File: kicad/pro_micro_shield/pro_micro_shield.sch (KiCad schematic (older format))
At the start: 14 parts, among them U0 ProMicro

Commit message: cleanup shield kicad project and readme
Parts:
- added H0, H1: MountingHole, MountingHole:MountingHole_2.2mm_M2, symbol Mechanical:MountingHole
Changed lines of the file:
@@
+	1    0    0    -1
+$EndComp
+$Comp
+L Mechanical:MountingHole H0
+U 1 1 5E6408C2
+P 7350 4550
+F 0 "H0" H 7450 4596 50  0000 L CNN
+F 1 "MountingHole" H 7450 4505 50  0000 L CNN
+F 2 "MountingHole:MountingHole_2.2mm_M2" H 7350 4550 50  0001 C CNN
+F 3 "~" H 7350 4550 50  0001 C CNN
+	1    7350 4550
+	1    0    0    -1
+$EndComp
+$Comp
+L Mechanical:MountingHole H1
+U 1 1 5E640F0D
+P 7350 4800
+F 0 "H1" H 7450 4846 50  0000 L CNN
+F 1 "MountingHole" H 7450 4755 50  0000 L CNN
+F 2 "MountingHole:MountingHole_2.2mm_M2" H 7350 4800 50  0001 C CNN
+F 3 "~" H 7350 4800 50  0001 C CNN
+	1    7350 4800
 	1    0    0    -1
 $EndComp

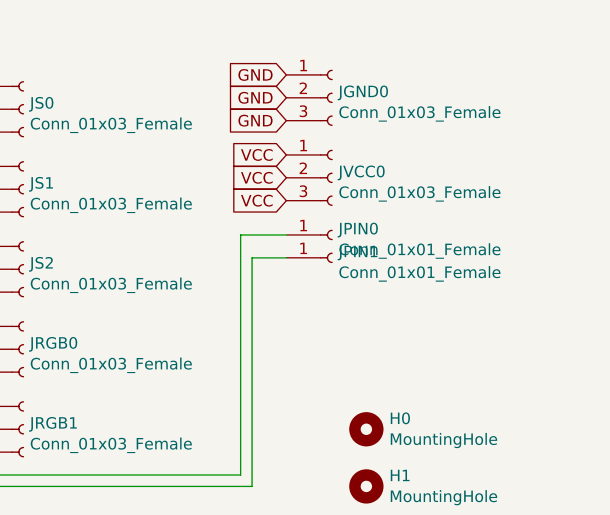
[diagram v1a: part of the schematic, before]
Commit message: cleanup shield kicad project and readme
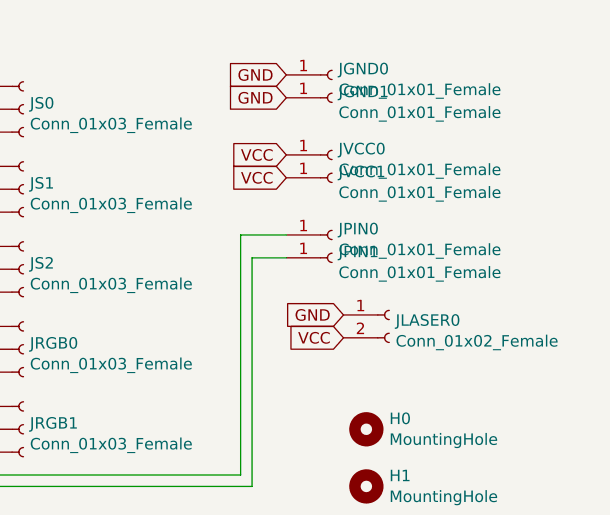
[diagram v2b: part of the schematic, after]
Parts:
- removed JGND0, JVCC0: Conn_01x03_Female, Connector_Wire:SolderWirePad_1x03_P3.175mm_Drill1mm, symbol Connector:Conn_01x03_Female
- added JGND0, JGND1, JVCC0, JVCC1: Conn_01x01_Female, Connector_Wire:SolderWirePad_1x01_Drill1mm, symbol Connector:Conn_01x01_Female
- added JLASER0: Conn_01x02_Female, Connector_Wire:SolderWirePad_1x02_P3.81mm_Drill1mm, symbol Connector:Conn_01x02_Female
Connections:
- net GND: now also JGND0.1 (Pin_1), JGND1.1 (Pin_1), JLASER0.1 (Pin_1)
- net VCC: now also JLASER0.2 (Pin_2), JVCC0.1 (Pin_1), JVCC1.1 (Pin_1)
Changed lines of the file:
@@
 Wire Wire Line
 	5200 5200 3150 5200
-$Comp
-L Connector:Conn_01x03_Female JGND0
-U 1 1 5E645A68
-P 7200 3100
-F 0 "JGND0" H 7228 3126 50  0000 L CNN
-F 1 "Conn_01x03_Female" H 7228 3035 50  0000 L CNN
-F 2 "Connector_Wire:SolderWirePad_1x03_P3.175mm_Drill1mm" H 7200 3100 50  0001 C CNN
-F 3 "~" H 7200 3100 50  0001 C CNN
-	1    7200 3100
-	1    0    0    -1
-$EndComp
-$Comp
-L Connector:Conn_01x03_Female JVCC0
-U 1 1 5E6468D3
-P 7200 3450
-F 0 "JVCC0" H 7228 3476 50  0000 L CNN
-F 1 "Conn_01x03_Female" H 7228 3385 50  0000 L CNN
-F 2 "Connector_Wire:SolderWirePad_1x03_P3.175mm_Drill1mm" H 7200 3450 50  0001 C CNN
-F 3 "~" H 7200 3450 50  0001 C CNN
-	1    7200 3450
-	1    0    0    -1
-$EndComp
 Text GLabel 7000 3000 0    50   Input ~ 0
 GND
 Text GLabel 7000 3100 0    50   Input ~ 0
 GND
-Text GLabel 7000 3200 0    50   Input ~ 0
-GND
 Text GLabel 7000 3350 0    50   Input ~ 0
 VCC
 Text GLabel 7000 3450 0    50   Input ~ 0
-VCC
-Text GLabel 7000 3550 0    50   Input ~ 0
 VCC
 Wire Wire Line
@@
 	1    0    0    -1
 $EndComp
+$Comp
+L Connector:Conn_01x02_Female JLASER0
+U 1 1 5E661891
+P 7450 4050
+F 0 "JLASER0" H 7478 4026 50  0000 L CNN
+F 1 "Conn_01x02_Female" H 7478 3935 50  0000 L CNN
+F 2 "Connector_Wire:SolderWirePad_1x02_P3.81mm_Drill1mm" H 7450 4050 50  0001 C CNN
+F 3 "~" H 7450 4050 50  0001 C CNN
+	1    7450 4050
+	1    0    0    -1
+$EndComp
+Text GLabel 7250 4150 0    50   Input ~ 0
+VCC
+Text GLabel 7250 4050 0    50   Input ~ 0
+GND
+$Comp
+L Connector:Conn_01x01_Female JGND0
+U 1 1 5E666EF2
+P 7200 3000
+F 0 "JGND0" H 7228 3026 50  0000 L CNN
+F 1 "Conn_01x01_Female" H 7228 2935 50  0000 L CNN
+F 2 "Connector_Wire:SolderWirePad_1x01_Drill1mm" H 7200 3000 50  0001 C CNN
+F 3 "~" H 7200 3000 50  0001 C CNN
+	1    7200 3000
+	1    0    0    -1
+$EndComp
+$Comp
+L Connector:Conn_01x01_Female JGND1
+U 1 1 5E667A92
+P 7200 3100
+F 0 "JGND1" H 7228 3126 50  0000 L CNN
+F 1 "Conn_01x01_Female" H 7228 3035 50  0000 L CNN
+F 2 "Connector_Wire:SolderWirePad_1x01_Drill1mm" H 7200 3100 50  0001 C CNN
+F 3 "~" H 7200 3100 50  0001 C CNN
+	1    7200 3100
+	1    0    0    -1
+$EndComp
+$Comp
+L Connector:Conn_01x01_Female JVCC0
+U 1 1 5E6684FC
+P 7200 3350
+F 0 "JVCC0" H 7228 3376 50  0000 L CNN
+F 1 "Conn_01x01_Female" H 7228 3285 50  0000 L CNN
+F 2 "Connector_Wire:SolderWirePad_1x01_Drill1mm" H 7200 3350 50  0001 C CNN
+F 3 "~" H 7200 3350 50  0001 C CNN
+	1    7200 3350
+	1    0    0    -1
+$EndComp
+$Comp
+L Connector:Conn_01x01_Female JVCC1
+U 1 1 5E6689E2
+P 7200 3450
+F 0 "JVCC1" H 7228 3476 50  0000 L CNN
+F 1 "Conn_01x01_Female" H 7228 3385 50  0000 L CNN
+F 2 "Connector_Wire:SolderWirePad_1x01_Drill1mm" H 7200 3450 50  0001 C CNN
+F 3 "~" H 7200 3450 50  0001 C CNN
+	1    7200 3450
+	1    0    0    -1
+$EndComp
